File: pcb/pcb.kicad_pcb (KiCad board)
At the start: 2 copper layers, 49 x 31 mm, 37 parts, among them J1 Conn_02x08_Odd_Even, J2 B2B-PH-K-S_LF__SN_, J3 USB_C_Receptacle, J4 Conn_01x04, Q1 MMUN2211LT1G, SW1 SW_SPST, U1 TPS61090, U2 MCP73871-1AA

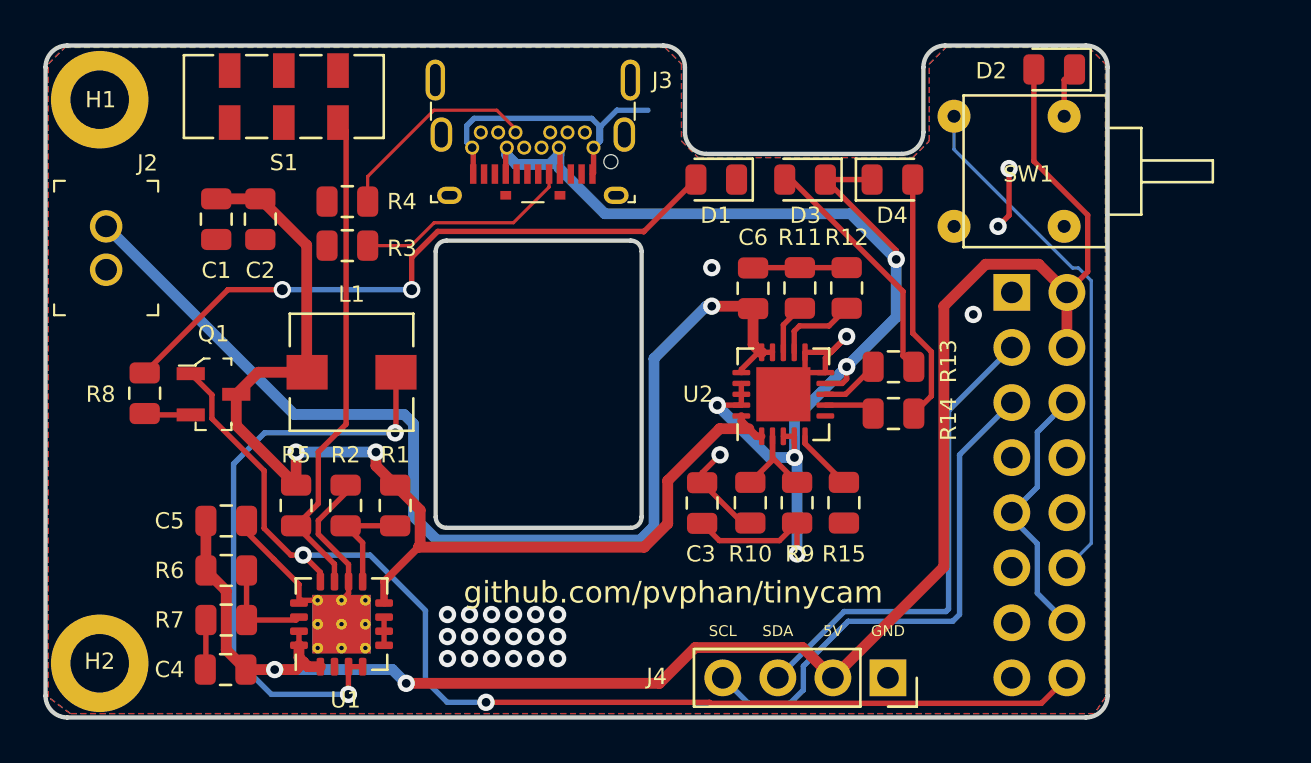
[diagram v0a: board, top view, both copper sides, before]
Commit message: updated PCB following boost converter design guidelines
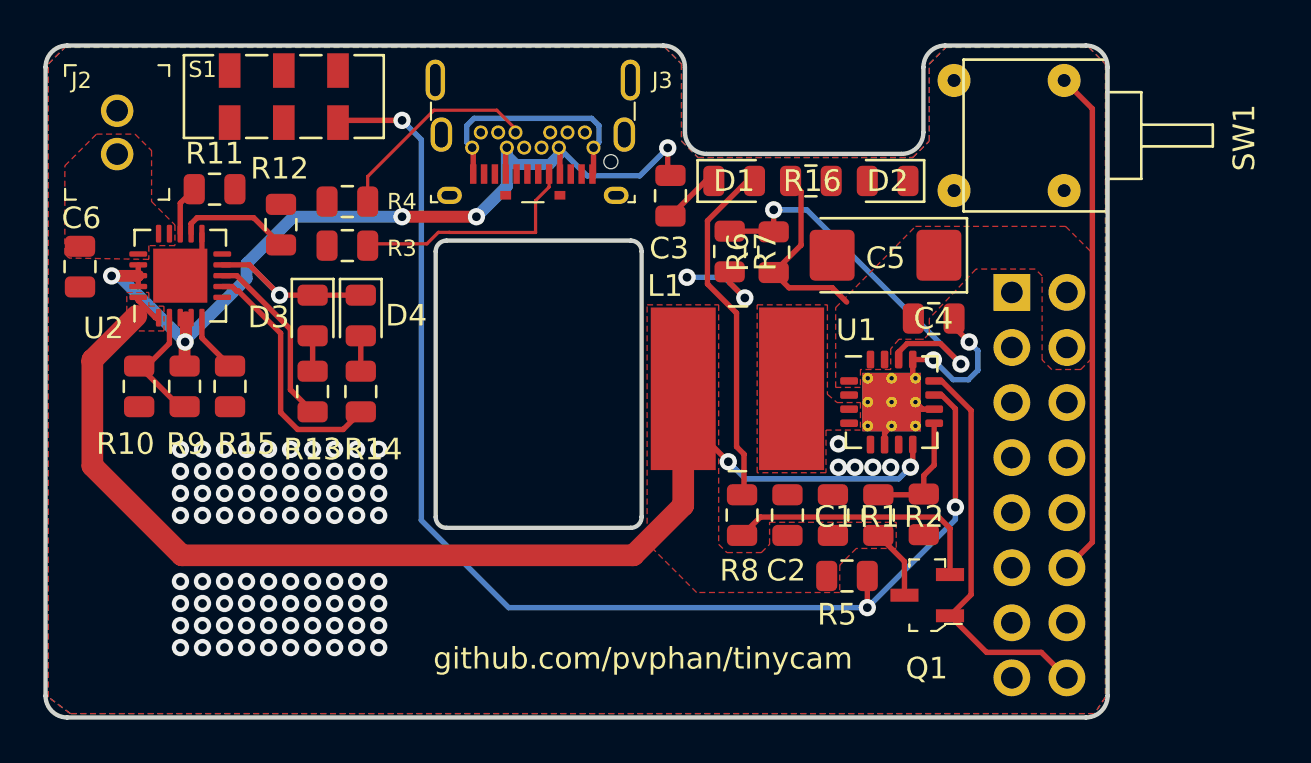
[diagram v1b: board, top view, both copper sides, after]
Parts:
- removed H1, H2: MountingHole, MountingHole:MountingHole_2.7mm_M2.5_ISO7380_Pad
- removed J4: Conn_01x04, Connector_PinSocket_2.54mm:PinSocket_1x04_P2.54mm_Vertical
- added R16: 1K, Resistor_SMD:R_0805_2012Metric, F.Cu at (186.3, 75.2)
- C5: footprint Capacitor_SMD:C_0805_2012Metric -> Capacitor_Tantalum_SMD:CP_EIA-6032-20_AVX-F
- L1: footprint Inductor_SMD:L_Wuerth_HCI-5040 -> Inductor_SMD:L_Wuerth_WE-PD2-Typ-L
- moved C4 36.5 mm to (192.0, 81.6), turned to 0 degrees
- moved Q1 34.2 mm to (191.7, 94.4), turned to 180 degrees
- moved C5 32.8 mm to (189.8, 78.7), turned to 180 degrees
- moved C1 31.6 mm to (187.3, 90.7), turned to 90 degrees
- moved C6 31.1 mm to (152.6, 79.2), turned to 270 degrees
- moved R6 29.2 mm to (184.6, 78.5), turned to 90 degrees
- moved R15 28.8 mm to (159.5, 84.7)
- moved R7 28.8 mm to (182.6, 78.5), turned to 270 degrees
- moved R9 28.8 mm to (157.4, 84.7), turned to 270 degrees
- moved R10 28.7 mm to (155.3, 84.7)
- moved U2 28.4 mm to (157.2, 79.6)
- moved R8 28.1 mm to (183.1, 90.7)
- moved C2 27.9 mm to (185.2, 90.7), turned to 90 degrees
- moved R11 27.4 mm to (158.8, 75.6), turned to 0 degrees
- moved U1 27.4 mm to (190.0, 85.4), turned to 0 degrees
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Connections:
- net Net-(C6-Pad1) renamed VLIPO
- D2 pad 2: 5.0V -> Net-(D2-Pad2)
- J1 pad 14: GND -> Net-(J1-Pad14)
- J1 pad 6: GND -> Net-(J1-Pad6)
- J1 pad 9: GND -> Net-(J1-Pad9)
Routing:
- net 5.0V: track 80.6 -> 8.88 mm, vias 2 -> 0
- net VLIPO: track 51.5 -> 0.00 mm, vias 1 -> 0
- net Net-(R5-Pad2): track 23.0 -> 57.6 mm, vias 0 -> 3
- net GND: track 64.6 -> 30.0 mm, vias 24 -> 89
- net PI_BCM_23: track 52.8 -> 18.7 mm, vias 2 -> 0
- net Net-(L1-Pad2): track 27.7 -> 0.00 mm, vias 2 -> 0
- net PI_BCM_3_SCL: track 24.5 -> 0.00 mm
- net PI_BCM_2_SDA: track 22.5 -> 0.00 mm
- net Net-(D1-Pad2): track 30.0 -> 16.3 mm, vias 2 -> 0
- net Net-(R6-Pad2): track 4.76 -> 18.4 mm, vias 0 -> 2
- net VBUS: track 63.2 -> 51.7 mm, vias 5 -> 6
- net Net-(Q1-Pad2): track 2.15 -> 12.3 mm
- net Net-(D4-Pad2): track 11.5 -> 1.63 mm
- net Net-(D3-Pad2): track 11.3 -> 1.63 mm
- net Net-(R14-Pad2): track 2.37 -> 11.6 mm
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- added copper zone on F.Cu, net 5.0V
- added copper zone on F.Cu, net Net-(L1-Pad2)
- added copper zone on F.Cu, net VBAT
- added copper zone on F.Cu, net VLIPO
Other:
- board text removed: "5V"
- board text removed: "GND"
- board text removed: "SCL"
- board text removed: "SDA"

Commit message: a little cleanup
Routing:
- net VBAT: track 62.0 -> 65.8 mm
- net Net-(D2-Pad2): track 0.00 -> 1.67 mm
- net Net-(J3-PadA5): track 11.0 -> 10.1 mm
- net GND: vias 89 -> 88

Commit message: updated schematic
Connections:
- D3 pad 1: VBUS -> Net-(D3-Pad1)
- D3 pad 2: Net-(D3-Pad2) -> VBUS
- D4 pad 1: VBUS -> Net-(D4-Pad1)
- D4 pad 2: Net-(D4-Pad2) -> VBUS
- J1 pad 6: Net-(J1-Pad6) -> GND
- R13 pad 1: Net-(D3-Pad2) -> Net-(D3-Pad1)
- R14 pad 1: Net-(D4-Pad2) -> Net-(D4-Pad1)
